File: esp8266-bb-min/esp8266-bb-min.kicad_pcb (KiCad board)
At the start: 2 copper layers, 31.8 x 39.4 mm, 25 parts, among them J1 Conn_01x02_Male, J2 Conn_01x04_Male, J3 Conn_01x04_Male, J4 Conn_01x06_Male, J5 Conn_01x04_Male, J6 Conn_01x04_Male, J7 Conn_01x02_Male, U1 LP38693MP-3.3, U2 ESP-12F

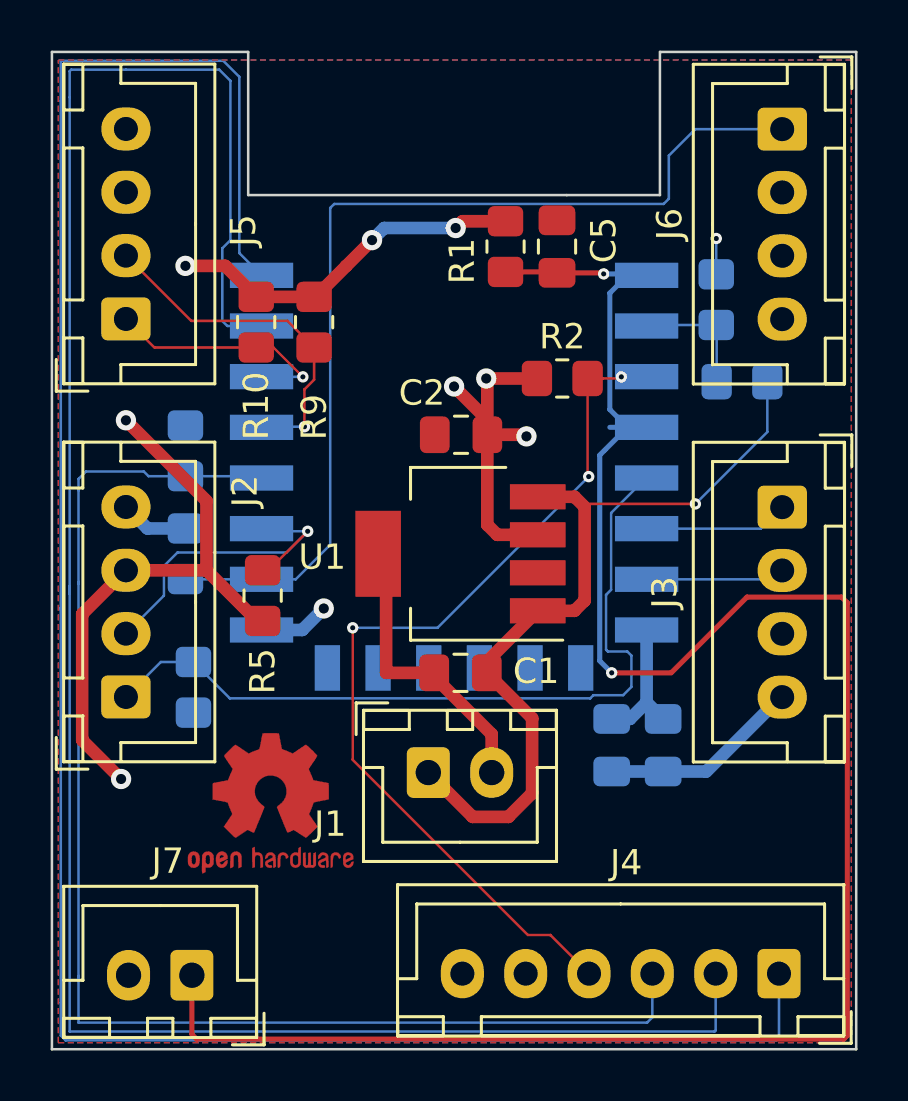
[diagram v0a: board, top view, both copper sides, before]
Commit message: pcb: corrected label positions
Signed-off-by: Dominik Laton <dominik.laton@web.de>
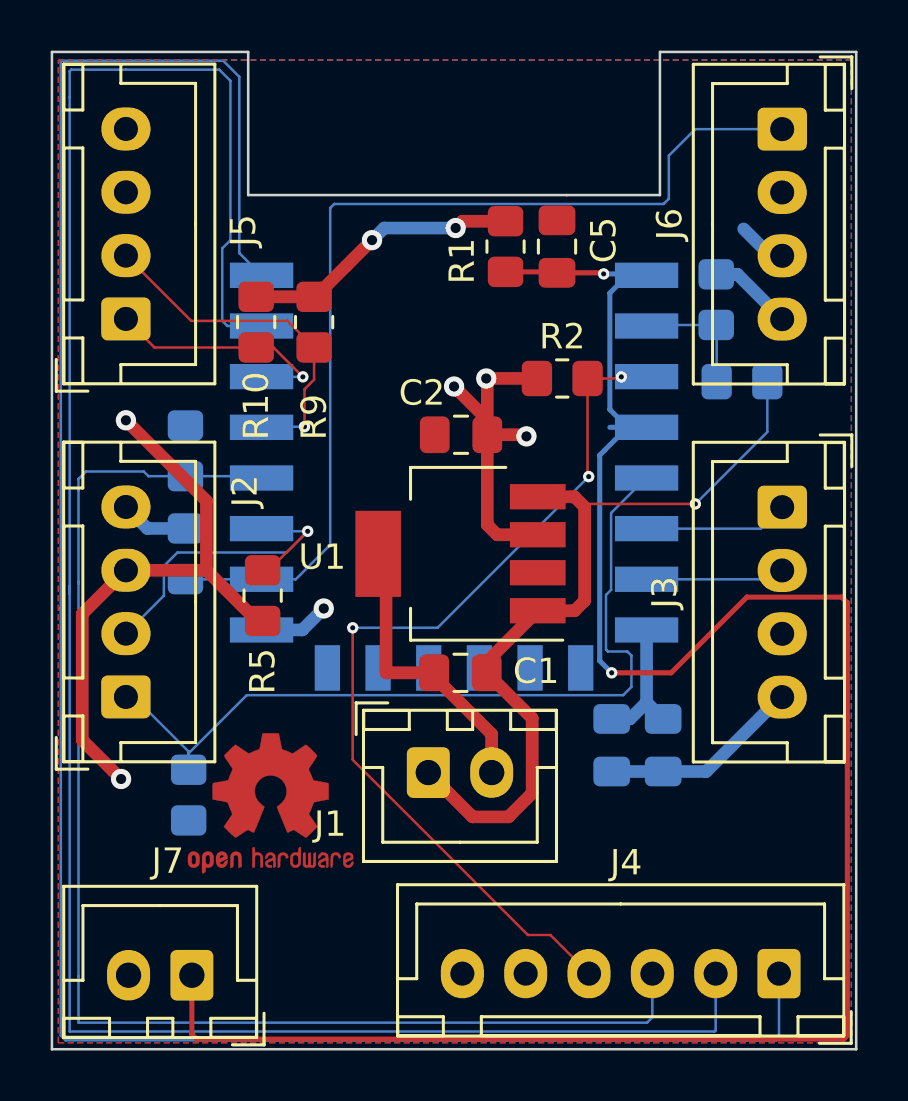
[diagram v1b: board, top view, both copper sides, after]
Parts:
- moved R6 4.26 mm to (103.1, 100.8)
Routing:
- net /ESP_GPIO14: track 31.1 -> 33.7 mm
- net -BATT: track 26.6 -> 28.6 mm, vias 2 -> 1
- net +3V3: track 56.8 -> 55.5 mm, vias 8 -> 7

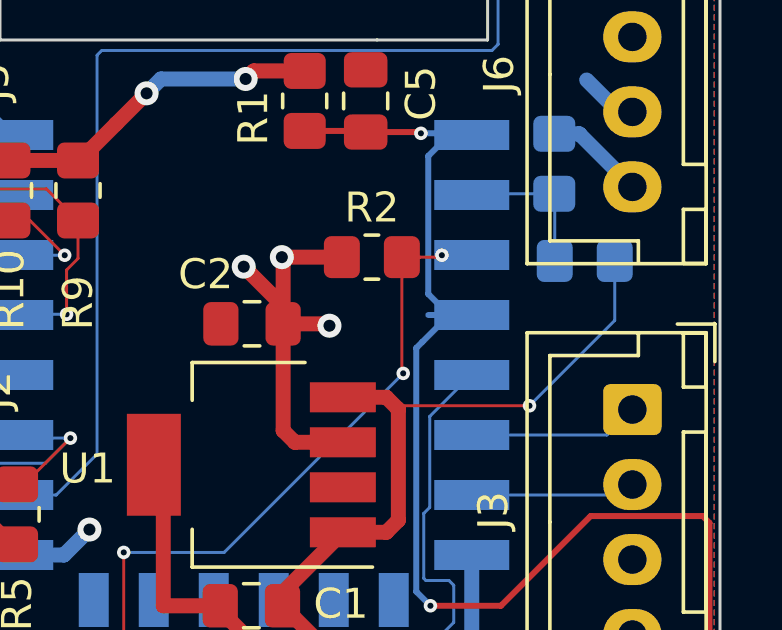
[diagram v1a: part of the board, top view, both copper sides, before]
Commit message: pcb: removed dangling track part
Signed-off-by: Dominik Laton <dominik.laton@web.de>
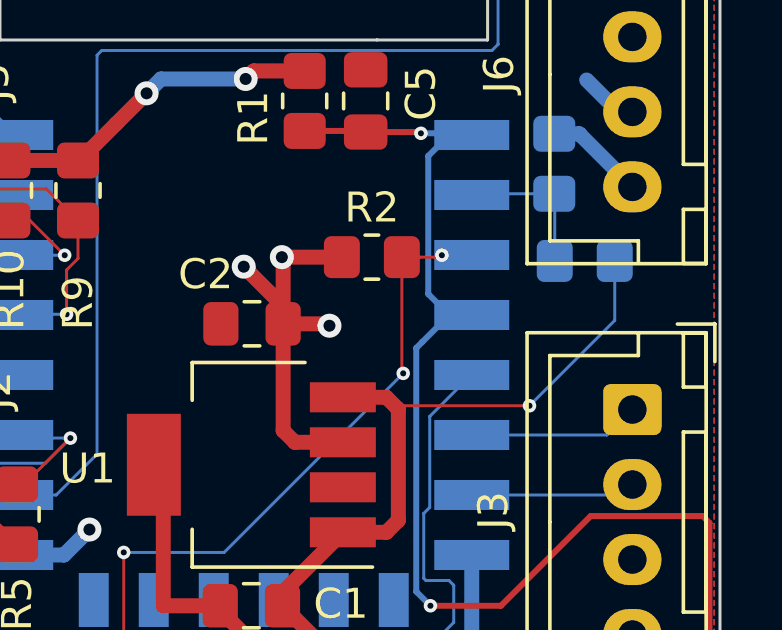
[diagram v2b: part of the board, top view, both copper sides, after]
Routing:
- net /~ESP_RST: track 83.2 -> 81.8 mm

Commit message: pcb: corrected resistor values for ADC
Signed-off-by: Dominik Laton <dominik.laton@web.de>
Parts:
- R7: value 15k -> 47k
- R8: value 39k -> 9k1
